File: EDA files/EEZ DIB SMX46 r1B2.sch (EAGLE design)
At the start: 158 parts, among them IC1 STM32F030C6T6, IC2 74HC1G126GW,125, IC3 M24C32-WMN6P, IC4 LP2985-33DBVR, IC5 74HC2G04GW,125, IC6 OPA2170, K1 FTR-C1GA012G-B05, K10 FTR-C1GA012G-B05, K11 FTR-C1GA012G-B05, K12 FTR-C1GA012G-B05, K13 FTR-C1GA012G-B05, K14 FTR-C1GA012G-B05, K15 FTR-C1GA012G-B05, K16 FTR-C1GA012G-B05, K17 FTR-C1GA012G-B05, K18 FTR-C1GA012G-B05, K19 FTR-C1GA012G-B05, K2 FTR-C1GA012G-B05, K20 FTR-C1GA012G-B05, K21 FTR-C1GA012G-B05, K22 FTR-C1GA012G-B05, K23 FTR-C1GA012G-B05, K24 FTR-C1GA012G-B05, K3 FTR-C1GA012G-B05, K4 FTR-C1GA012G-B05, K5 FTR-C1GA012G-B05, K6 FTR-C1GA012G-B05, K7 FTR-C1GA012G-B05, K8 FTR-C1GA012G-B05, K9 FTR-C1GA012G-B05, Q1 2N7002, Q10 2N7002, Q11 2N7002, Q12 2N7002, Q13 2N7002, Q14 2N7002, Q15 2N7002, Q16 2N7002, Q17 2N7002, Q18 2N7002, Q19 2N7002, Q2 2N7002, Q20 2N7002, Q21 2N7002, Q22 2N7002, Q23 2N7002, Q24 2N7002, Q25 2N7002, Q3 2N7002, Q4 2N7002, Q5 2N7002, Q6 2N7002, Q7 2N7002, Q8 2N7002, Q9 2N7002, X1 N.C., X2 77317-104-28LF, X3 691327310016, X4 691327310016

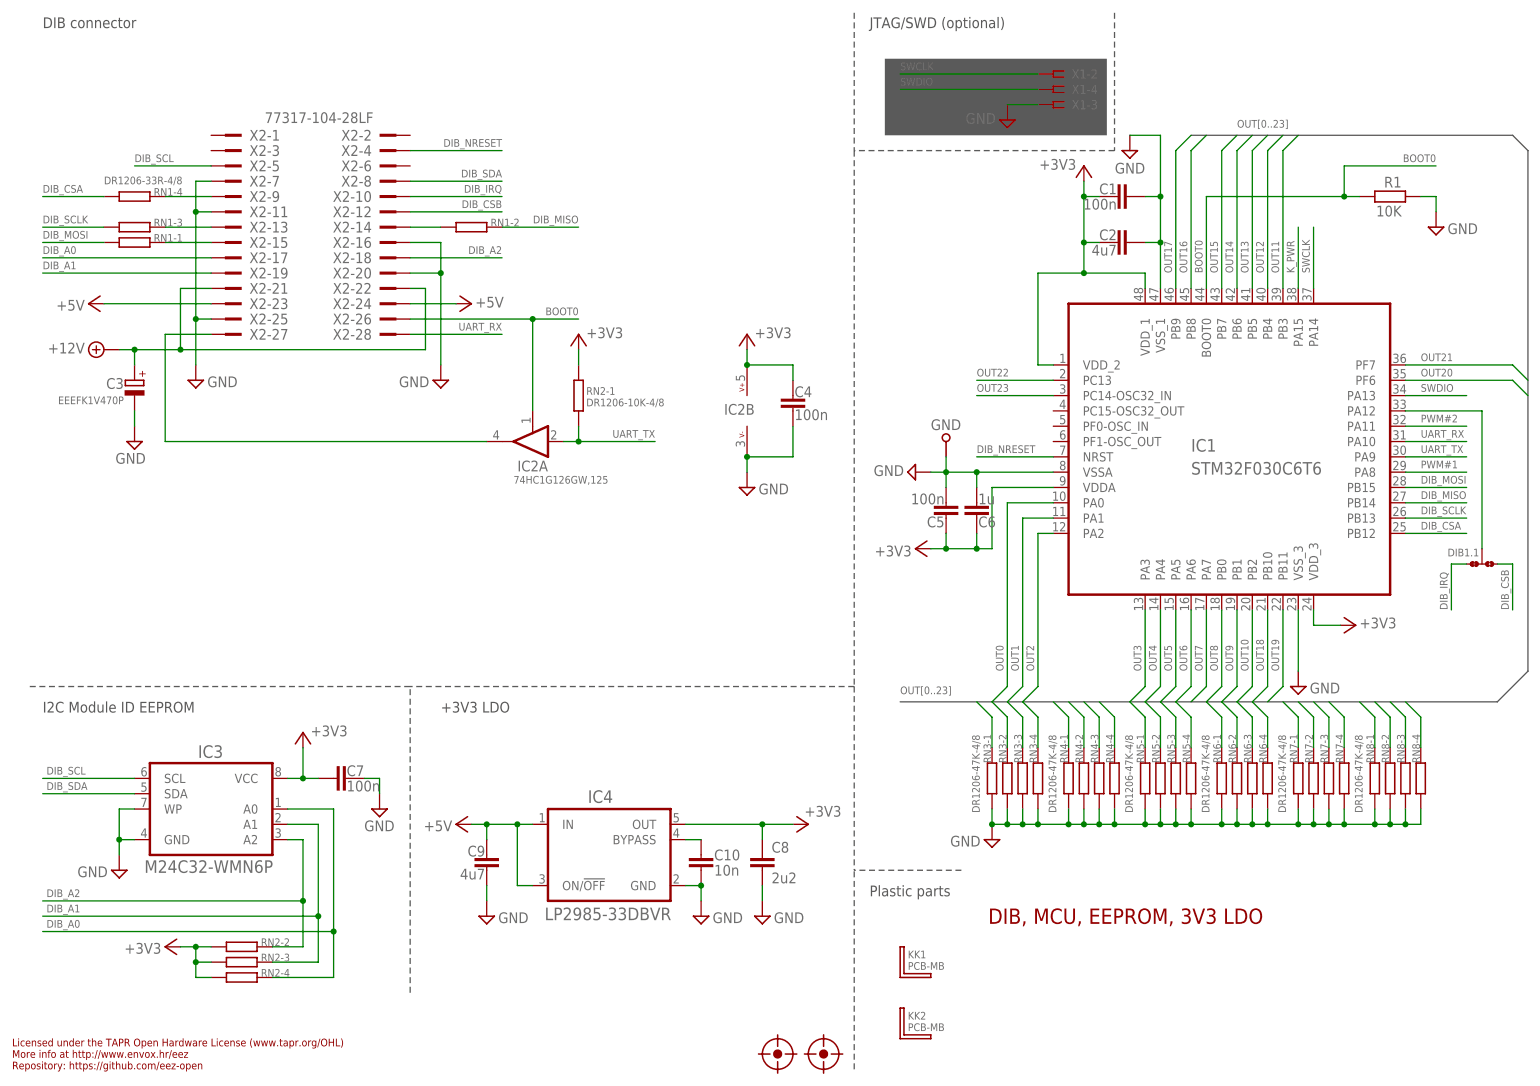
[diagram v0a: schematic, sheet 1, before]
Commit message: front panel labels update
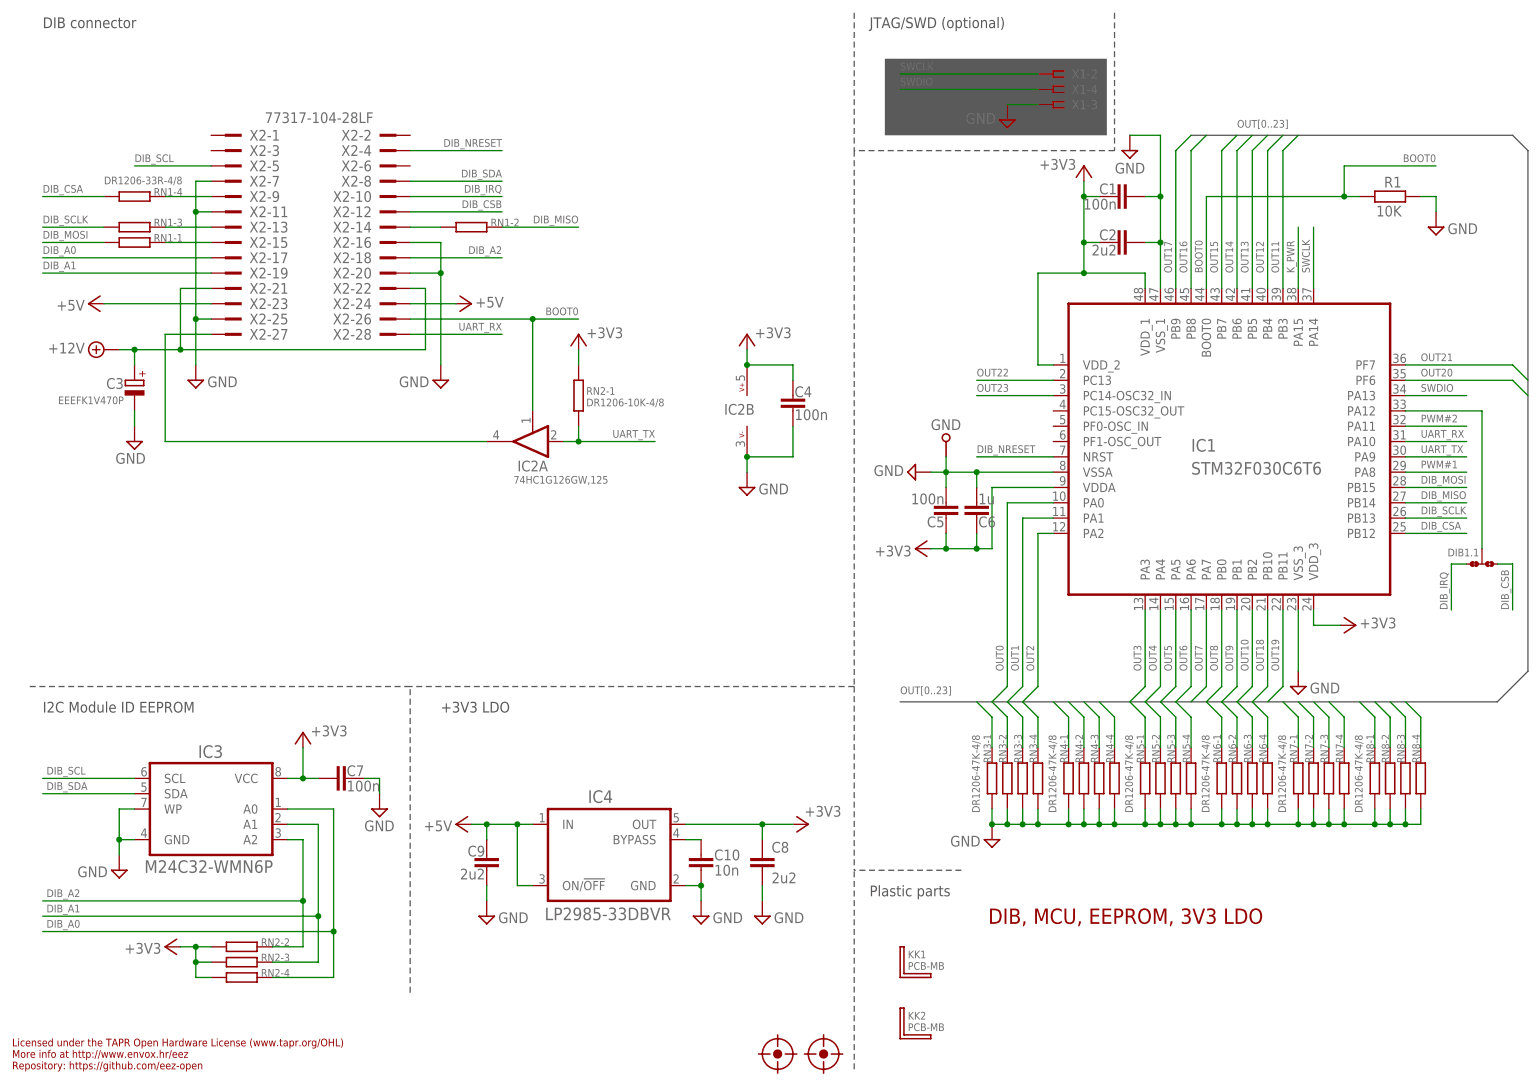
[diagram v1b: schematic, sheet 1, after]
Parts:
- C2, C9: value 4u7 -> 2u2
- IC6: value OPA2170 -> OPA2990IDR
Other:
- note added: "X5A"
- note added: "X5B"
- note added: "X6A"
- note added: "X6B"
- note removed: "Y5A"
- note removed: "Y5B"
- note removed: "Y6A"
- note removed: "Y6B"
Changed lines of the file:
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@@
 <part name="SUPPLY36" library="supply2" deviceset="GND" device=""/>
 <part name="+3V8" library="supply1" deviceset="+3V3" device=""/>
-<part name="IC6" library="EEZ_Lib1" deviceset="TL072" device="SOIC8" value="OPA2170"/>
+<part name="IC6" library="EEZ_Lib1" deviceset="TL072" device="SOIC8" value="OPA2990IDR"/>
 <part name="R3" library="rcl" deviceset="R-EU_" device="R0805" value="10K"/>
 <part name="R4" library="rcl" deviceset="R-EU_" device="R0805" value="4K7"/>
@@
 <part name="SUPPLY49" library="supply2" deviceset="GND" device=""/>
 <part name="C1" library="rcl" deviceset="C-EU" device="C0603" value="100n"/>
-<part name="C2" library="rcl" deviceset="C-EU" device="C0805" value="4u7"/>
+<part name="C2" library="rcl" deviceset="C-EU" device="C0805" value="2u2"/>
 <part name="SUPPLY61" library="supply2" deviceset="GND" device=""/>
 <part name="+3V4" library="supply1" deviceset="+3V3" device=""/>
@@
 <part name="C3" library="EEZ_Lib1" deviceset="ECAP" device="PANASONIC_H" value="EEEFK1V470P"/>
 <part name="SUPPLY45" library="supply2" deviceset="GND" device=""/>
-<part name="C9" library="rcl" deviceset="C-EU" device="C0805" value="4u7"/>
+<part name="C9" library="rcl" deviceset="C-EU" device="C0805" value="2u2"/>
 <part name="RN2" library="EEZ_Lib1" deviceset="R_ARRAY4" device="" value="DR1206-10K-4/8"/>
 <part name="+3V5" library="supply1" deviceset="+3V3" device=""/>
@@
 <circle x="214.63" y="163.83" radius="0.635" width="0.1524" layer="101"/>
 <circle x="214.63" y="161.29" radius="0.635" width="0.1524" layer="101"/>
-<text x="204.47" y="164.465" size="1.4224" layer="101" rot="R180">X3B</text>
-<text x="217.17" y="165.735" size="1.4224" layer="101">Y2A</text>
+<text x="204.47" y="164.465" size="1.4224" layer="101" rot="R180">Y2B</text>
+<text x="217.17" y="165.735" size="1.4224" layer="101">X2A</text>
 <wire x1="162.56" y1="129.54" x2="162.56" y2="177.8" width="0.1524" layer="97" style="shortdash"/>
 <wire x1="205.74" y1="172.72" x2="215.9" y2="172.72" width="0.1524" layer="101"/>
 <text x="193.04" y="174.625" size="1.778" layer="101">2 x 16-pin front panel connector</text>
-<text x="217.17" y="160.655" size="1.4224" layer="101">Y3A</text>
+<text x="217.17" y="160.655" size="1.4224" layer="101">X3A</text>
 <wire x1="215.9" y1="172.72" x2="215.9" y2="167.64" width="0.1524" layer="101"/>
 <circle x="207.01" y="156.21" radius="0.635" width="0.1524" layer="101"/>
 <circle x="214.63" y="156.21" radius="0.635" width="0.1524" layer="101"/>
-<text x="204.47" y="161.925" size="1.4224" layer="101" rot="R180">X2A</text>
+<text x="204.47" y="161.925" size="1.4224" layer="101" rot="R180">Y3A</text>
 <circle x="207.01" y="158.75" radius="0.635" width="0.1524" layer="101"/>
 <circle x="214.63" y="158.75" radius="0.635" width="0.1524" layer="101"/>
-<text x="217.17" y="170.815" size="1.4224" layer="101">Y1A</text>
-<text x="204.47" y="172.085" size="1.4224" layer="101" rot="R180">X4A</text>
+<text x="217.17" y="170.815" size="1.4224" layer="101">X1A</text>
+<text x="204.47" y="172.085" size="1.4224" layer="101" rot="R180">Y1A</text>
 <circle x="214.63" y="153.67" radius="0.635" width="0.1524" layer="101"/>
-<text x="217.17" y="163.195" size="1.4224" layer="101">Y2B</text>
+<text x="217.17" y="163.195" size="1.4224" layer="101">X2B</text>
 <circle x="207.01" y="153.67" radius="0.635" width="0.1524" layer="101"/>
 <circle x="207.01" y="150.495" radius="0.635" width="0.1524" layer="101"/>
@@
 <circle x="214.63" y="142.875" radius="0.635" width="0.1524" layer="101"/>
 <circle x="214.63" y="140.335" radius="0.635" width="0.1524" layer="97"/>
-<text x="204.47" y="167.005" size="1.4224" layer="101" rot="R180">X3A</text>
-<text x="217.17" y="168.275" size="1.4224" layer="101">Y1B</text>
-<text x="204.47" y="169.545" size="1.4224" layer="101" rot="R180">X4B</text>
+<text x="204.47" y="167.005" size="1.4224" layer="101" rot="R180">Y2A</text>
+<text x="217.17" y="168.275" size="1.4224" layer="101">X1B</text>
+<text x="204.47" y="169.545" size="1.4224" layer="101" rot="R180">Y1B</text>
 <wire x1="215.9" y1="167.64" x2="215.9" y2="162.56" width="0.1524" layer="101"/>
 <wire x1="215.9" y1="162.56" x2="215.9" y2="157.48" width="0.1524" layer="101"/>
@@
 <wire x1="205.74" y1="146.685" x2="215.9" y2="146.685" width="0.1524" layer="101" style="shortdash"/>
 <wire x1="205.74" y1="141.605" x2="215.9" y2="141.605" width="0.1524" layer="101" style="shortdash"/>
-<text x="204.47" y="156.845" size="1.4224" layer="101" rot="R180">X1A</text>
-<text x="204.47" y="154.305" size="1.4224" layer="101" rot="R180">X1B</text>
-<text x="204.47" y="159.385" size="1.4224" layer="101" rot="R180">X2B</text>
+<text x="204.47" y="156.845" size="1.4224" layer="101" rot="R180">Y4A</text>
+<text x="204.47" y="154.305" size="1.4224" layer="101" rot="R180">Y4B</text>
+<text x="204.47" y="159.385" size="1.4224" layer="101" rot="R180">Y3B</text>
 <text x="204.47" y="148.59" size="1.4224" layer="101" rot="R180">AGND</text>
 <text x="204.47" y="146.05" size="1.4224" layer="101" rot="R180">DAC2</text>
@@
 <text x="204.47" y="133.35" size="1.4224" layer="101" rot="R180">K-NC</text>
 <text x="204.47" y="135.89" size="1.4224" layer="101" rot="R180">K-COMM</text>
-<text x="217.17" y="158.115" size="1.4224" layer="101">Y3B</text>
-<text x="217.17" y="153.035" size="1.4224" layer="101">Y4B</text>
-<text x="217.17" y="155.575" size="1.4224" layer="101">Y4A</text>
-<text x="217.17" y="149.86" size="1.4224" layer="101">Y5A</text>
-<text x="217.17" y="144.78" size="1.4224" layer="101">Y6A</text>
-<text x="217.17" y="147.32" size="1.4224" layer="101">Y5B</text>
-<text x="217.17" y="142.24" size="1.4224" layer="101">Y6B</text>
+<text x="217.17" y="158.115" size="1.4224" layer="101">X3B</text>
+<text x="217.17" y="153.035" size="1.4224" layer="101">X4B</text>
+<text x="217.17" y="155.575" size="1.4224" layer="101">X4A</text>
+<text x="217.17" y="149.86" size="1.4224" layer="101">X5A</text>
+<text x="217.17" y="144.78" size="1.4224" layer="101">X6A</text>
+<text x="217.17" y="147.32" size="1.4224" layer="101">X5B</text>
+<text x="217.17" y="142.24" size="1.4224" layer="101">X6B</text>
 <text x="217.17" y="137.16" size="1.4224" layer="101">K-NO</text>
 <text x="217.17" y="139.7" size="1.4224" layer="97">N.C.</text>

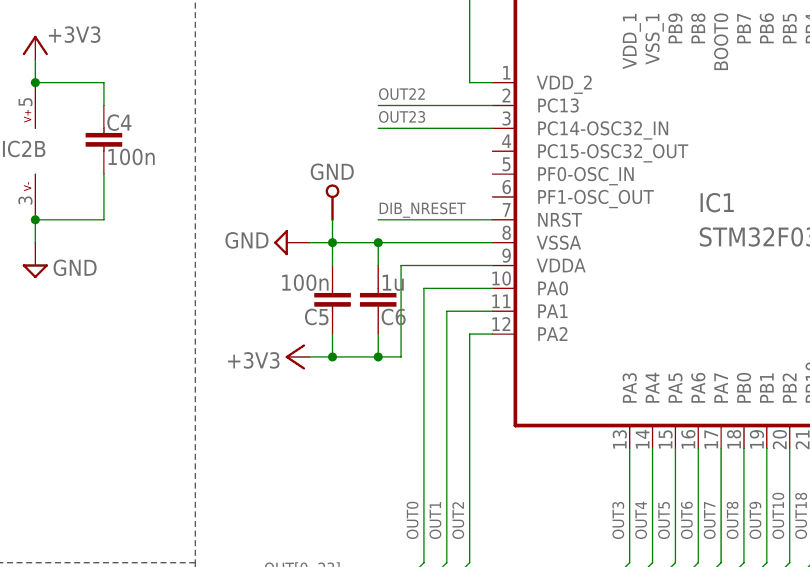
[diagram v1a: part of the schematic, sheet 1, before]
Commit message: C6 value
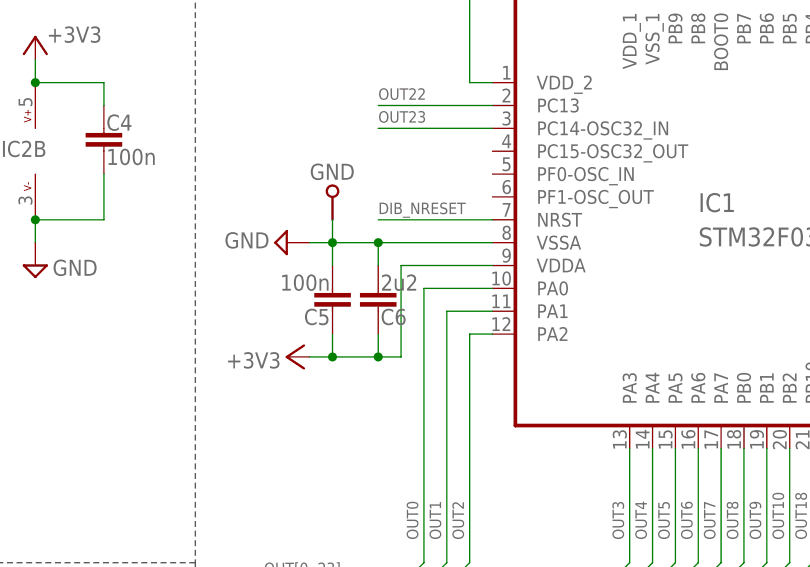
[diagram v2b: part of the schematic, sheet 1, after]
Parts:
- C6: value 1u -> 2u2
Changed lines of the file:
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@@
 <part name="R1" library="rcl" deviceset="R-EU_" device="R0805" value="10K"/>
 <part name="SUPPLY63" library="supply2" deviceset="GND" device=""/>
-<part name="C6" library="rcl" deviceset="C-EU" device="C0805" value="1u"/>
+<part name="C6" library="rcl" deviceset="C-EU" device="C0805" value="2u2"/>
 <part name="C5" library="rcl" deviceset="C-EU" device="C0603" value="100n"/>
 <part name="+3V2" library="supply1" deviceset="+3V3" device=""/>
